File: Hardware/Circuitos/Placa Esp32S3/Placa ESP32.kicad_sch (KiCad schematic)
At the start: 9 parts, among them J1 Conn_01x04, J3 ESP32-S3-Touch-LCD-3.5B, J4 Conn_01x02, J8 Conn_01x02

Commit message: Placa ESP32 - Cambio de huella bornera
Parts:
- J8: footprint Connector_Molex:Molex_KK-254_AE-6410-02A_1x02_P2.54mm_Vertical -> Connector_Molex:Molex_KK-254_AE-6410-04A_1x04_P2.54mm_Vertical
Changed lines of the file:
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@@
 			)
 		)
-		(property "Footprint" "Connector_Molex:Molex_KK-254_AE-6410-02A_1x02_P2.54mm_Vertical"
+		(property "Footprint" "Connector_Molex:Molex_KK-254_AE-6410-04A_1x04_P2.54mm_Vertical"
 			(at 99.06 67.31 0)
 			(hide yes)

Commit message: Placa ESP - Actualizacion bornera
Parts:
- added J2: Conn_01x04, Connector_Molex:Molex_KK-254_AE-6410-04A_1x04_P2.54mm_Vertical, symbol Connector_Generic:Conn_01x04
- J8: footprint Connector_Molex:Molex_KK-254_AE-6410-04A_1x04_P2.54mm_Vertical -> Connector_Molex:Molex_KK-254_AE-6410-02A_1x02_P2.54mm_Vertical
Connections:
- net GPIO11 (MQ-2): now also J2.2 (Pin_2)
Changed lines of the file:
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@@
+		)
+	)
+	(wire
+		(pts
+			(xy 131.445 74.295) (xy 145.415 74.295)
+		)
+		(stroke
+			(width 0)
+			(type default)
 		)
 	)
@@
 			)
 			(justify left bottom)
+		)
+	)
+	(label "GPIO11 (MQ-2)"
+		(at 131.445 74.295 180)
+		(effects
+			(font
+				(size 1.27 1.27)
+			)
+			(justify right bottom)
 		)
 	)
@@
 			)
 		)
-		(property "Footprint" "Connector_Molex:Molex_KK-254_AE-6410-04A_1x04_P2.54mm_Vertical"
+		(property "Footprint" "Connector_Molex:Molex_KK-254_AE-6410-02A_1x02_P2.54mm_Vertical"
 			(at 99.06 67.31 0)
 			(hide yes)
@@
 					(unit 1)
 				)
+			)
+		)
+	)
+	(symbol
+		(lib_id "Connector_Generic:Conn_01x04")
+		(at 150.495 74.295 0)
+		(unit 1)
+		(body_style 1)
+		(exclude_from_sim no)
+		(in_bom yes)
+		(on_board yes)
+		(in_pos_files yes)
+		(dnp no)
+		(fields_autoplaced yes)
+		(property "Reference" "J2"
+			(at 153.67 74.2949 0)
+			(show_name no)
+			(do_not_autoplace no)
+			(effects
+				(font
+					(size 1.27 1.27)
+				)
+				(justify left)
+			)
+		)
+		(property "Value" "Conn_01x04"
+			(at 153.67 76.8349 0)
+			(show_name no)
+			(do_not_autoplace no)
+			(effects
+				(font
+					(size 1.27 1.27)
+				)
+				(justify left)
+			)
+		)
+		(property "Footprint" "Connector_Molex:Molex_KK-254_AE-6410-04A_1x04_P2.54mm_Vertical"
+			(at 150.495 74.295 0)
+			(hide yes)
+			(show_name no)
+			(do_not_autoplace no)
+			(effects
+				(font
+					(size 1.27 1.27)
+				)
+			)
+		)
+		(property "Datasheet" ""
+			(at 150.495 74.295 0)
+			(hide yes)
+			(show_name no)
+			(do_not_autoplace no)
+			(effects
+				(font
+					(size 1.27 1.27)
+				)
+			)
+		)
+		(property "Description" "Generic connector, single row, 01x04, script generated (kicad-library-utils/schlib/autogen/connector/)"
+			(at 150.495 74.295 0)
+			(hide yes)
+			(show_name no)
+			(do_not_autoplace no)
+			(effects
+				(font
+					(size 1.27 1.27)
+				)
+			)
+		)
+		(pin "1"
+		)
+		(pin "3"
+		)
+		(pin "4"
+		)
+		(pin "2"
+		)
+		(instances
+			(project "Placa ESP32"
+				(path "/61d975b5-0f12-484d-9c90-802e15475eba"
+					(reference "J2")
+					(unit 1)
+				)

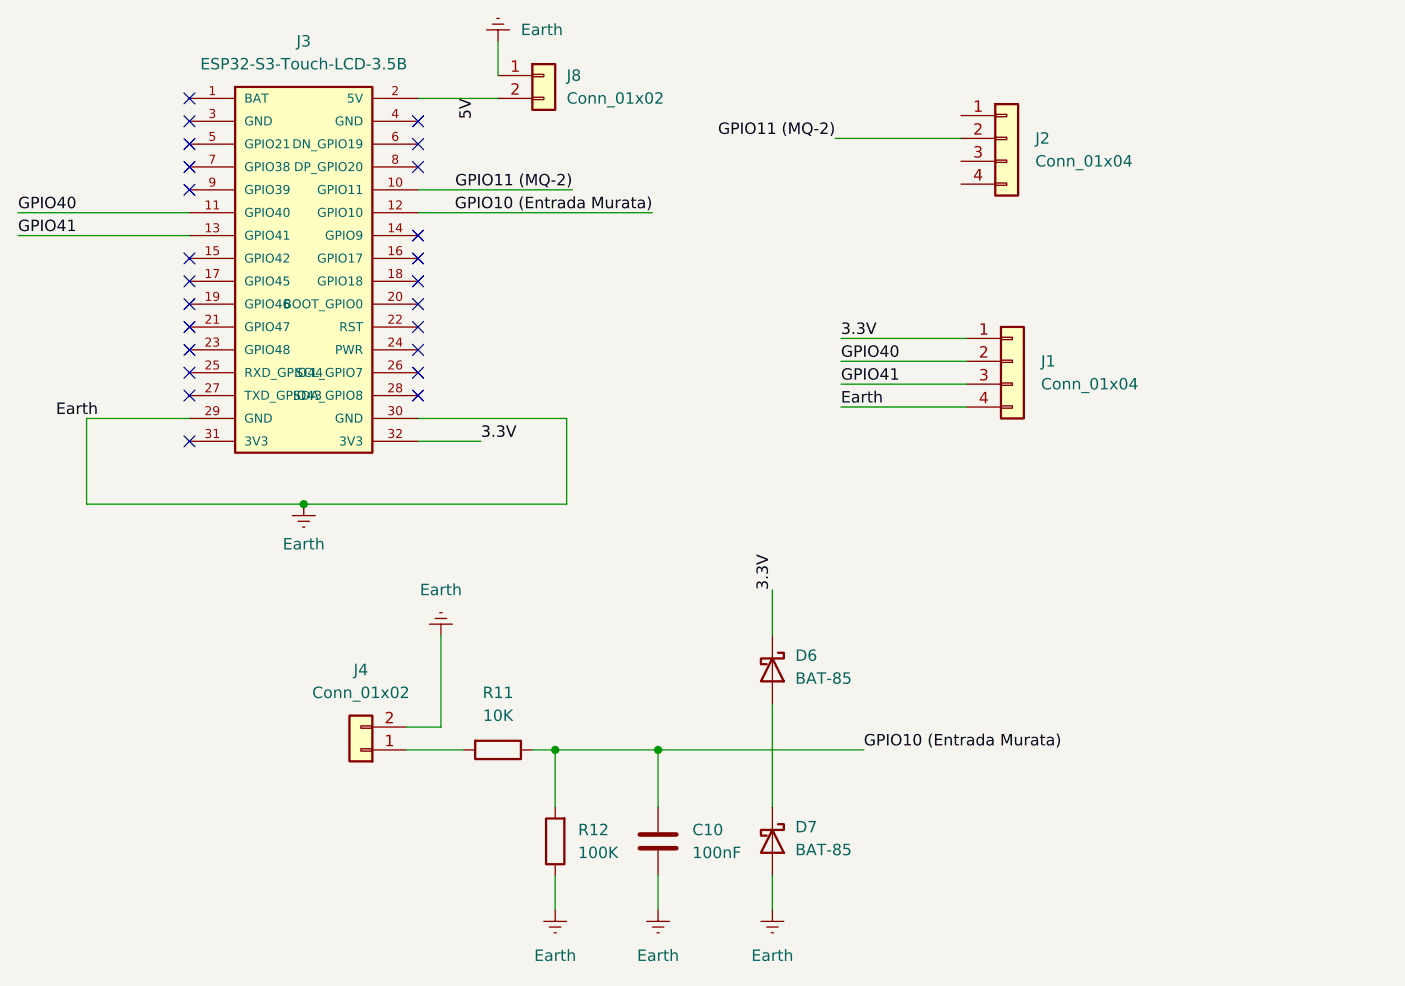
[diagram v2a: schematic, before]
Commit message: Placa ESP32 - Colocar componentes en la PCB
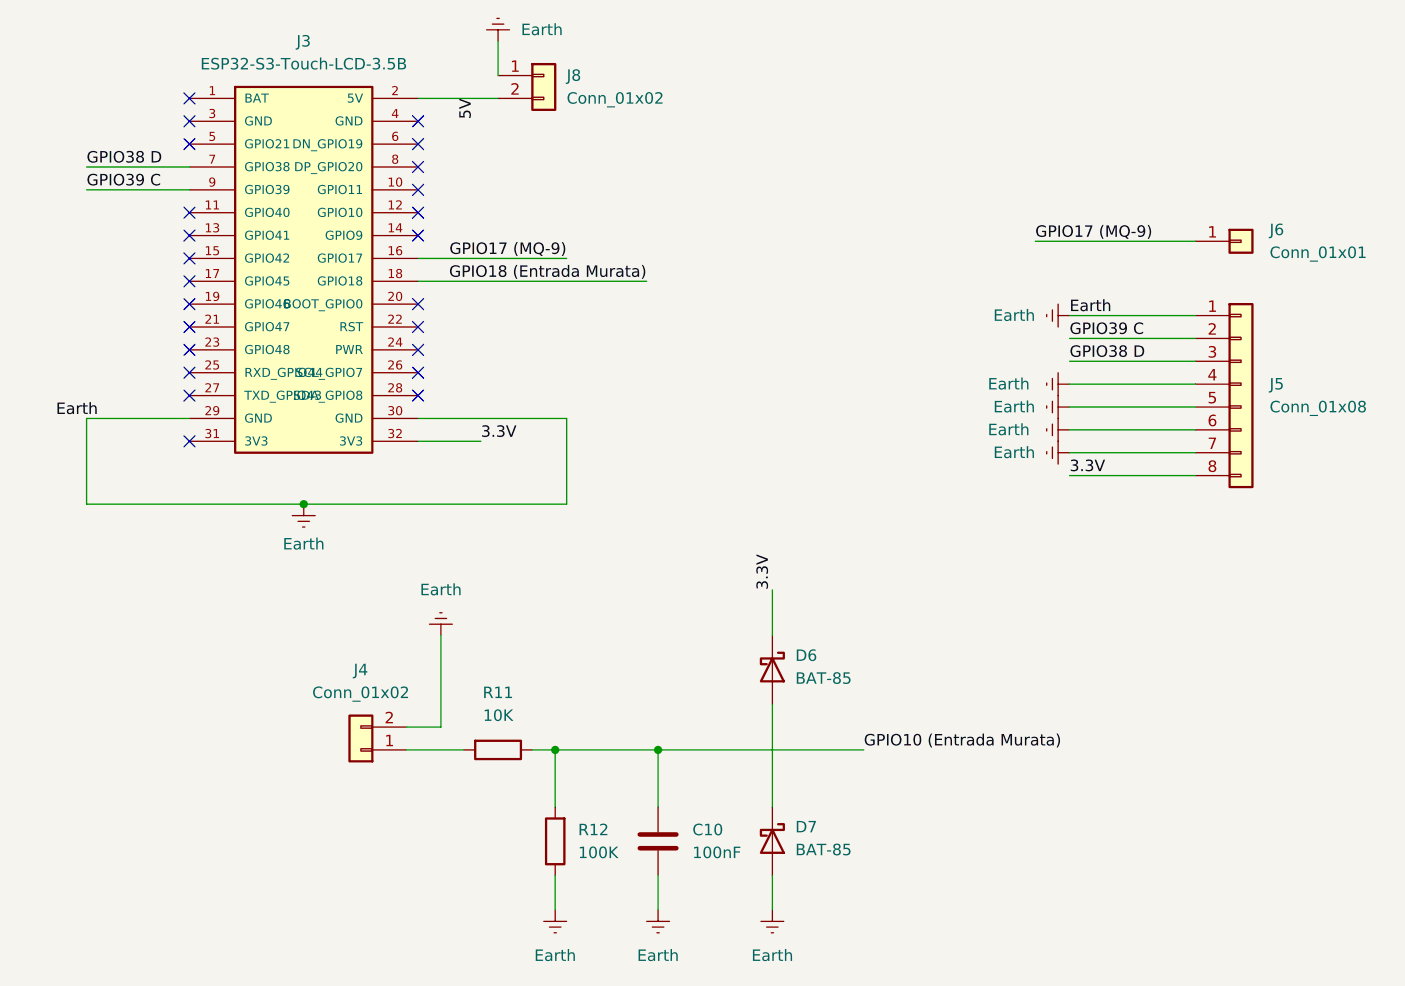
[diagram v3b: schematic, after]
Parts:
- removed J1, J2: Conn_01x04, Connector_Molex:Molex_KK-254_AE-6410-04A_1x04_P2.54mm_Vertical, symbol Connector_Generic:Conn_01x04
- added J5: Conn_01x08, Connector_RJ:RJ45_Amphenol_54602-x08_Horizontal, symbol Connector_Generic:Conn_01x08
- added J6: Conn_01x01, Connector_PinHeader_2.00mm:PinHeader_1x01_P2.00mm_Vertical, symbol Connector_Generic:Conn_01x01
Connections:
- net 3.3V: now also J5.8 (Pin_8)
- net Earth: now also J5.1 (Pin_1), J5.4 (Pin_4), J5.5 (Pin_5), J5.6 (Pin_6), J5.7 (Pin_7)
- net GPIO10 (Entrada Murata): no longer J3.12 (GPIO10)
- net GPIO17 (MQ-9): now reaches J3.16 (GPIO17)
- net GPIO17 (MQ-9): now also J6.1 (Pin_1)
- net GPIO18 (Entrada Murata): now reaches J3.18 (GPIO18)
- net GPIO38 D: now reaches J3.7 (GPIO38)
- net GPIO38 D: now also J5.3 (Pin_3)
- net GPIO39 C: now reaches J3.9 (GPIO39)
- net GPIO39 C: now also J5.2 (Pin_2)
- net GPIO11 (MQ-2): no longer names the net of J3.10 (GPIO11)
- net GPIO40: no longer names the net of J3.11 (GPIO40)
- net GPIO41: no longer names the net of J3.13 (GPIO41)

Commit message: Placa ESP32 - Corrección de pista
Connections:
- net GPIO10 (Entrada Murata) is gone; now on net GPIO18 (Entrada Murata): C10.1, R11.1, R12.2
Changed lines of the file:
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@@
 		)
 	)
-	(label "GPIO10 (Entrada Murata)"
+	(label "GPIO18 (Entrada Murata)"
 		(at 134.62 142.24 0)
 		(effects
